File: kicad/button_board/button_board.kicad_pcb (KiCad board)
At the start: 2 copper layers, 50.8 x 38.1 mm, 9 parts, among them J1 Conn_01x05_Male, SW1 apem-3eth9-15.0, SW2 apem-3eth9-15.0, SW3 apem-3eth9-15.0, SW4 apem-3eth9-15.0

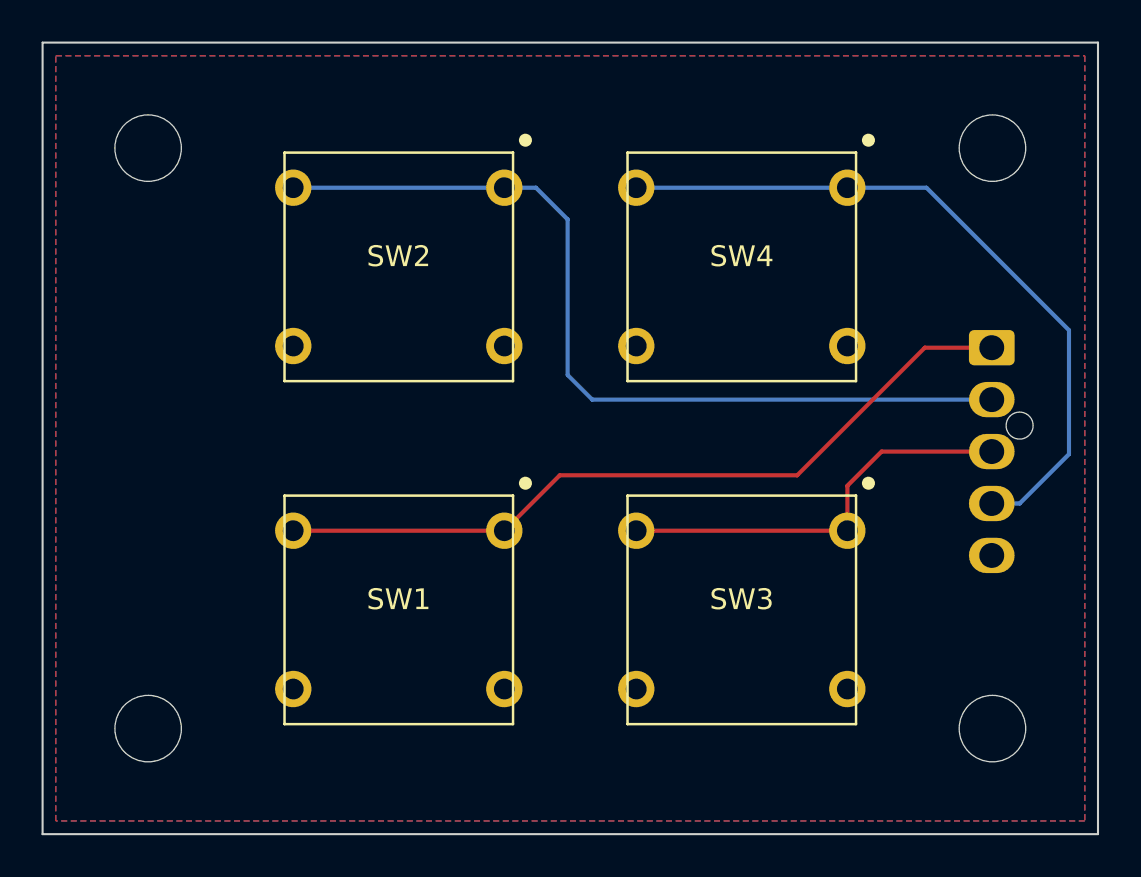
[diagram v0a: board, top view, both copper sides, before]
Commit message: increase track/clearance size
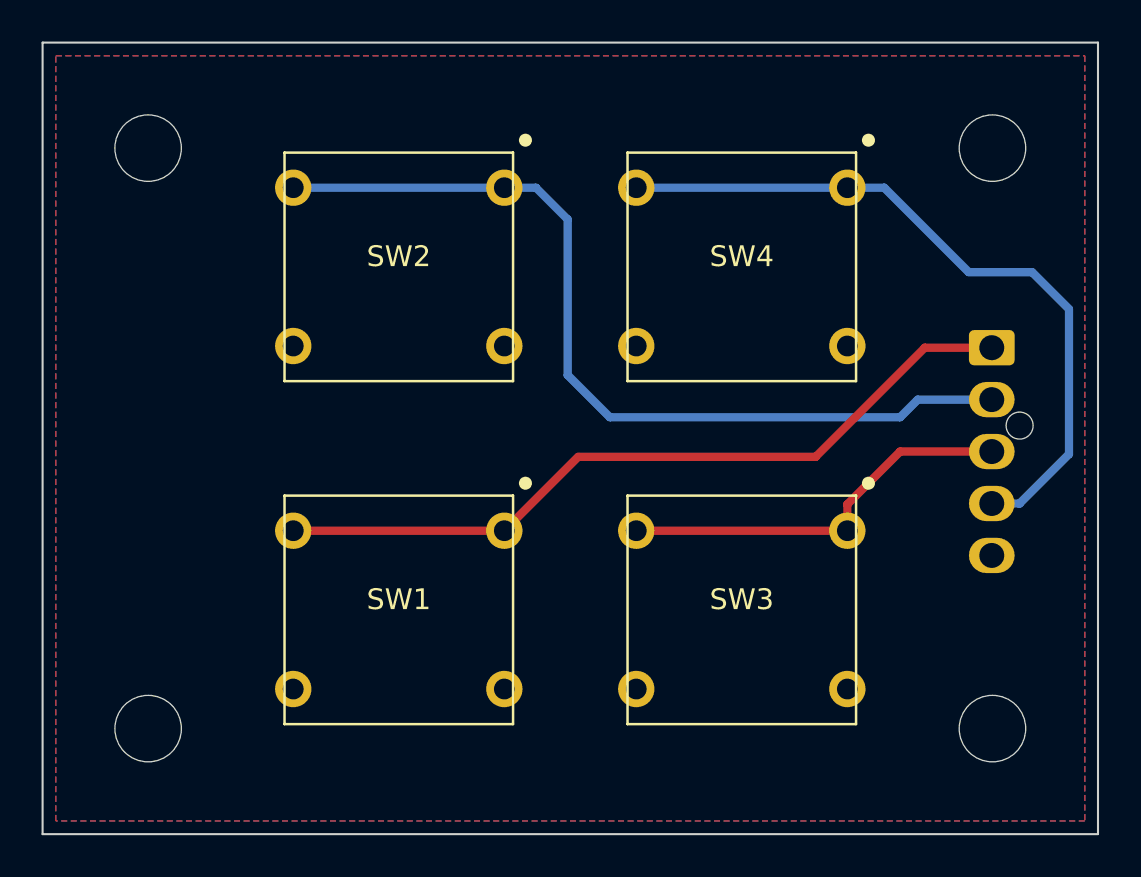
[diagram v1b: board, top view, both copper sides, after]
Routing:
- net /HOUR_DOWN: track 42.2 -> 42.9 mm
- net /MIN_DOWN: track 34.3 -> 34.9 mm
- net /MIN_UP: track 20.0 -> 19.4 mm
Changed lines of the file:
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@@
   (gr_line (start 120.65 118.11) (end 171.45 118.11)
     (stroke (width 0.1) (type default)) (layer "Edge.Cuts"))
-  (segment (start 156.972 100.838) (end 163.115 94.695) (width 0.2) (layer "F.Cu") (net 1))
-  (segment (start 145.542 100.838) (end 156.972 100.838) (width 0.2) (layer "F.Cu") (net 1))
-  (segment (start 142.875 103.505) (end 145.542 100.838) (width 0.2) (layer "F.Cu") (net 1))
-  (segment (start 132.715 103.505) (end 142.875 103.505) (width 0.2) (layer "F.Cu") (net 1))
-  (segment (start 163.115 94.695) (end 166.337005 94.695) (width 0.2) (layer "F.Cu") (net 1))
-  (segment (start 147.106 97.195) (end 166.337005 97.195) (width 0.2) (layer "B.Cu") (net 2))
-  (segment (start 132.715 86.995) (end 142.875 86.995) (width 0.2) (layer "B.Cu") (net 2))
-  (segment (start 144.399 86.995) (end 145.923 88.519) (width 0.2) (layer "B.Cu") (net 2))
-  (segment (start 145.923 88.519) (end 145.923 96.012) (width 0.2) (layer "B.Cu") (net 2))
-  (segment (start 142.875 86.995) (end 144.399 86.995) (width 0.2) (layer "B.Cu") (net 2))
-  (segment (start 145.923 96.012) (end 147.106 97.195) (width 0.2) (layer "B.Cu") (net 2))
-  (segment (start 161.036 99.695) (end 166.337005 99.695) (width 0.2) (layer "F.Cu") (net 3))
-  (segment (start 159.385 103.505) (end 159.385 101.346) (width 0.2) (layer "F.Cu") (net 3))
-  (segment (start 159.385 101.346) (end 161.036 99.695) (width 0.2) (layer "F.Cu") (net 3))
-  (segment (start 149.225 103.505) (end 159.385 103.505) (width 0.2) (layer "F.Cu") (net 3))
-  (segment (start 170.053 99.822) (end 167.68 102.195) (width 0.2) (layer "B.Cu") (net 4))
-  (segment (start 170.053 93.853) (end 170.053 99.822) (width 0.2) (layer "B.Cu") (net 4))
-  (segment (start 159.385 86.995) (end 163.195 86.995) (width 0.2) (layer "B.Cu") (net 4))
-  (segment (start 149.225 86.995) (end 159.385 86.995) (width 0.2) (layer "B.Cu") (net 4))
-  (segment (start 167.68 102.195) (end 166.337005 102.195) (width 0.2) (layer "B.Cu") (net 4))
-  (segment (start 163.195 86.995) (end 170.053 93.853) (width 0.2) (layer "B.Cu") (net 4))
+  (segment (start 157.861 99.949) (end 163.115 94.695) (width 0.4) (layer "F.Cu") (net 1))
+  (segment (start 142.875 103.505) (end 146.431 99.949) (width 0.4) (layer "F.Cu") (net 1))
+  (segment (start 163.115 94.695) (end 166.337005 94.695) (width 0.4) (layer "F.Cu") (net 1))
+  (segment (start 146.431 99.949) (end 157.861 99.949) (width 0.4) (layer "F.Cu") (net 1))
+  (segment (start 132.715 103.505) (end 142.875 103.505) (width 0.4) (layer "F.Cu") (net 1))
+  (segment (start 161.925 98.044) (end 162.774 97.195) (width 0.4) (layer "B.Cu") (net 2))
+  (segment (start 142.875 86.995) (end 144.399 86.995) (width 0.4) (layer "B.Cu") (net 2))
+  (segment (start 132.715 86.995) (end 142.875 86.995) (width 0.4) (layer "B.Cu") (net 2))
+  (segment (start 144.399 86.995) (end 145.923 88.519) (width 0.4) (layer "B.Cu") (net 2))
+  (segment (start 145.923 96.012) (end 147.955 98.044) (width 0.4) (layer "B.Cu") (net 2))
+  (segment (start 147.955 98.044) (end 161.925 98.044) (width 0.4) (layer "B.Cu") (net 2))
+  (segment (start 162.774 97.195) (end 166.337005 97.195) (width 0.4) (layer "B.Cu") (net 2))
+  (segment (start 145.923 88.519) (end 145.923 96.012) (width 0.4) (layer "B.Cu") (net 2))
+  (segment (start 161.925 99.695) (end 166.337005 99.695) (width 0.4) (layer "F.Cu") (net 3))
+  (segment (start 159.385 102.235) (end 161.925 99.695) (width 0.4) (layer "F.Cu") (net 3))
+  (segment (start 159.385 103.505) (end 159.385 102.235) (width 0.4) (layer "F.Cu") (net 3))
+  (segment (start 149.225 103.505) (end 159.385 103.505) (width 0.4) (layer "F.Cu") (net 3))
+  (segment (start 159.385 86.995) (end 161.163 86.995) (width 0.4) (layer "B.Cu") (net 4))
+  (segment (start 167.68 102.195) (end 166.337005 102.195) (width 0.4) (layer "B.Cu") (net 4))
+  (segment (start 170.053 99.822) (end 167.68 102.195) (width 0.4) (layer "B.Cu") (net 4))
+  (segment (start 165.227 91.059) (end 168.275 91.059) (width 0.4) (layer "B.Cu") (net 4))
+  (segment (start 149.225 86.995) (end 159.385 86.995) (width 0.4) (layer "B.Cu") (net 4))
+  (segment (start 161.163 86.995) (end 165.227 91.059) (width 0.4) (layer "B.Cu") (net 4))
+  (segment (start 170.053 92.837) (end 170.053 99.822) (width 0.4) (layer "B.Cu") (net 4))
+  (segment (start 168.275 91.059) (end 170.053 92.837) (width 0.4) (layer "B.Cu") (net 4))
   (zone (net 5) (net_name "GND") (layer "F.Cu") (hatch edge 0.508)
     (connect_pads (clearance 0.508))

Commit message: dfm
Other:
- outline, holes or cut-outs redrawn
- board text added: "London Gentleman Labs"

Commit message: update
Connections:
- J1 pad 1: /HOUR_UP -> /HOUR_DOWN
- J1 pad 2: /HOUR_DOWN -> /HOUR_UP
- J1 pad 3: /MIN_UP -> /MIN_DOWN
- J1 pad 4: /MIN_DOWN -> /MIN_UP
- SW1 pad 1: /HOUR_UP -> /HOUR_DOWN
- SW1 pad 2: /HOUR_UP -> /HOUR_DOWN
- SW2 pad 1: /HOUR_DOWN -> /HOUR_UP
- SW2 pad 2: /HOUR_DOWN -> /HOUR_UP
- SW3 pad 1: /MIN_UP -> /MIN_DOWN
- SW3 pad 2: /MIN_UP -> /MIN_DOWN
- SW4 pad 1: /MIN_DOWN -> /MIN_UP
- SW4 pad 2: /MIN_DOWN -> /MIN_UP
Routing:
- net /MIN_UP: track 19.4 -> 34.9 mm
- net /MIN_DOWN: track 34.9 -> 19.4 mm
- net /HOUR_UP: track 37.3 -> 42.9 mm
- net /HOUR_DOWN: track 42.9 -> 37.3 mm
